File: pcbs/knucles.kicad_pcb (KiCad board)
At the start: 2 copper layers, 130.3 x 107.9 mm, 152 parts

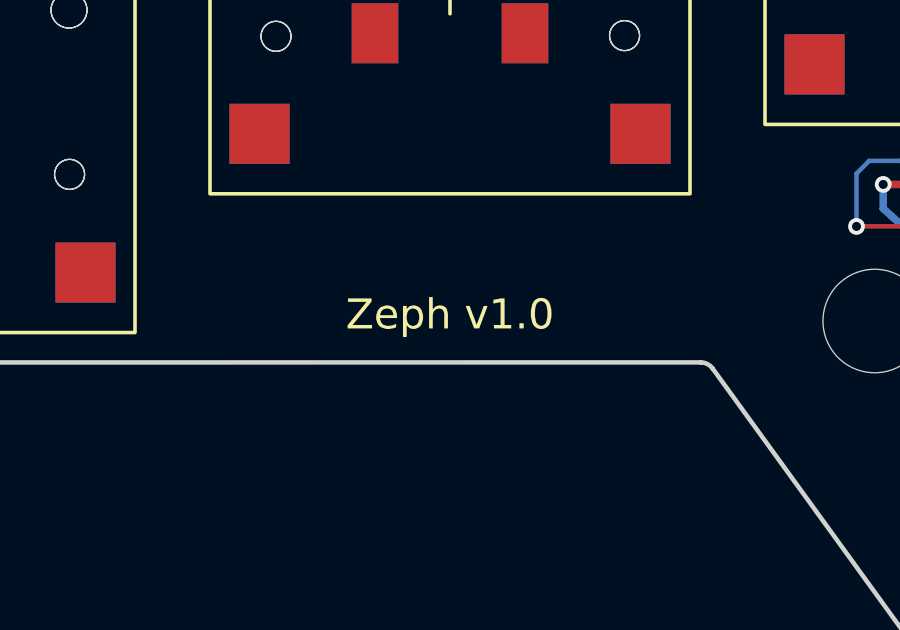
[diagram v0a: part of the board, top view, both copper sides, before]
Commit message: feat: renamed zeph board to knuckles (#1)
* feat: renamed zeph

* fix: github action board name

* chore: more renaming
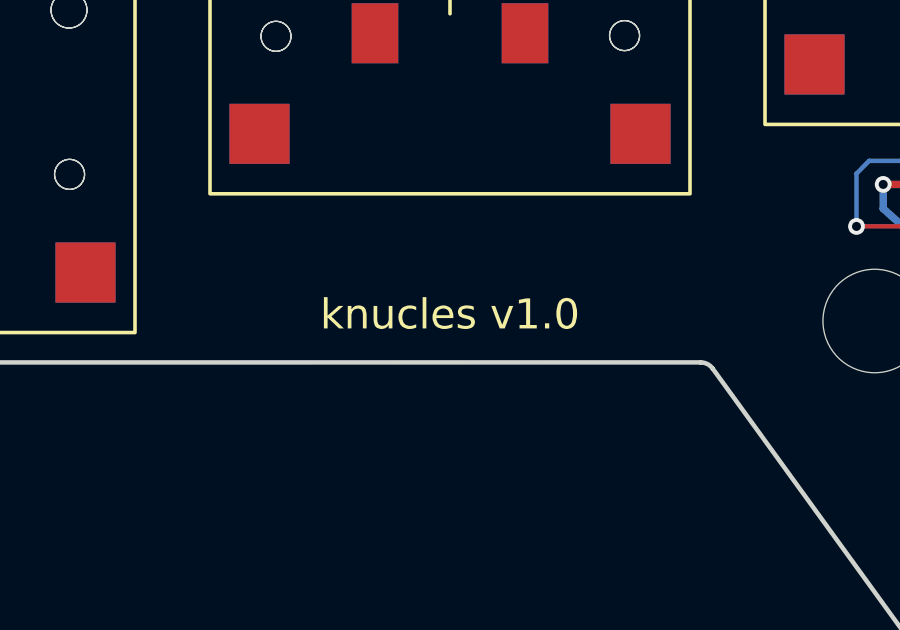
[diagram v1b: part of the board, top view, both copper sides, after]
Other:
- board text added: "knucles v1.0"
- board text removed: "Zeph v1.0"
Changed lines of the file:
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@@
   (paper "A3")
   (title_block
-    (title "zeph")
-    (date "2025-03-02")
+    (title "knucles")
+    (date "2025-03-17")
     (rev "0.2")
-    (company "ceoloide")
+    (company "fcoury")
   )
   (layers
@@
   (segment (start 215.90430500000002 86.635) (end 215.303695 86.635) (width 0.25) (layer "B.Cu"))
   (segment (start 215.303695 86.635) (end 214.798695 87.14) (width 0.25) (layer "B.Cu"))
-  (gr_text "Zeph v1.0"
+  (gr_text "knucles v1.0"
     (at 137 107.4 0)
     (layer "F.SilkS" )
@@
     )
   )
-  (gr_text "Zeph v1.0"
+  (gr_text "knucles v1.0"
     (at 137 107.4 0)
     (layer "B.SilkS" )
